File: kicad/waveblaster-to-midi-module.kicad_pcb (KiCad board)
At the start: 2 copper layers, 33 x 101 mm, 14 parts, among them J1 Midi Out, J2 Midi In, J3 Right In, J4 Left In, J5 Right Out, J6 Left Out, J7 Wavetable Input, U1 H11L1

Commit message: final board revision, update readme
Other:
- board text added: "Waveblaster Breakout Card v1.0 by Nikitalita"
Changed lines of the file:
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@@
     (property "Sheetfile" "waveblaster-to-midi-module.kicad_sch")
     (property "Sheetname" "")
-    (attr exclude_from_pos_files)
+    (attr exclude_from_pos_files exclude_from_bom)
     (fp_text reference "H1" (at 0 -4.2) (layer "F.SilkS") hide
       (effects (font (size 1 1) (thickness 0.15)))
@@
     (property "Sheetfile" "waveblaster-to-midi-module.kicad_sch")
     (property "Sheetname" "")
-    (attr through_hole)
+    (attr through_hole exclude_from_pos_files exclude_from_bom)
     (fp_text reference "U1" (at -0.01 -5.6 270) (layer "F.SilkS")
       (effects (font (size 1 1) (thickness 0.15)))
@@
     (property "Sheetfile" "waveblaster-to-midi-module.kicad_sch")
     (property "Sheetname" "")
-    (attr through_hole)
+    (attr through_hole exclude_from_pos_files exclude_from_bom)
     (fp_text reference "D1" (at 7.0893 0.08 270) (layer "F.SilkS")
       (effects (font (size 1 1) (thickness 0.15)))
@@
     (property "Sheetfile" "waveblaster-to-midi-module.kicad_sch")
     (property "Sheetname" "")
-    (attr through_hole)
+    (attr through_hole exclude_from_pos_files exclude_from_bom)
     (fp_text reference "J2" (at 0.1 -6.45 90) (layer "F.SilkS")
       (effects (font (size 1 1) (thickness 0.15)))
@@
     (property "Sheetfile" "waveblaster-to-midi-module.kicad_sch")
     (property "Sheetname" "")
-    (attr through_hole)
+    (attr through_hole exclude_from_pos_files exclude_from_bom)
     (fp_text reference "R2" (at -2.03 -0.01 90) (layer "F.SilkS")
       (effects (font (size 1 1) (thickness 0.15)))
@@
     (property "Sheetfile" "waveblaster-to-midi-module.kicad_sch")
     (property "Sheetname" "")
-    (attr through_hole)
+    (attr through_hole exclude_from_pos_files exclude_from_bom)
     (fp_text reference "J5" (at -5.43 -6.03) (layer "F.SilkS")
       (effects (font (size 1.006465 1.006465) (thickness 0.15)))
@@
     (pad "2" thru_hole oval (at -8.5 0) (size 3.4 1.7) (drill oval 2.3 1) (layers *.Cu *.Mask)
       (net 15 "WT_AUDIO_R_IN") (pintype "passive"))
-    (model "${KIPRJMOD}/Library.3dshapes/CUI_DEVICES_RCJ-042.step"
+    (model "${KIPRJMOD}/Library.3dshapes/CUI_DEVICES_RCJ-042.step" hide
       (offset (xyz -10.1 0 6.5))
       (scale (xyz 1 1 1))
@@
     (property "Sheetfile" "waveblaster-to-midi-module.kicad_sch")
     (property "Sheetname" "")
-    (attr through_hole)
+    (attr through_hole exclude_from_pos_files exclude_from_bom)
     (fp_text reference "R1" (at -1.79 -0.34) (layer "F.SilkS")
       (effects (font (size 1 1) (thickness 0.15)))
@@
     (property "Sheetfile" "waveblaster-to-midi-module.kicad_sch")
     (property "Sheetname" "")
-    (attr through_hole)
+    (attr through_hole exclude_from_pos_files exclude_from_bom)
     (fp_text reference "J6" (at -5.27 -5.93) (layer "F.SilkS")
       (effects (font (size 1.006465 1.006465) (thickness 0.15)))
@@
     (pad "2" thru_hole oval (at -8.5 0) (size 3.4 1.7) (drill oval 2.3 1) (layers *.Cu *.Mask)
       (net 12 "WT_AUDIO_L_IN") (pintype "passive"))
-    (model "${KIPRJMOD}/Library.3dshapes/CUI_DEVICES_RCJ-043.step"
+    (model "${KIPRJMOD}/Library.3dshapes/CUI_DEVICES_RCJ-043.step" hide
       (offset (xyz -10.1 0 6.5))
       (scale (xyz 1 1 1))
@@
       (xy 156.98 153)
     ) (layer "Edge.Cuts") (width 0.1) (fill none))
+  (gr_text "Waveblaster Breakout Card\nv1.0\nby Nikitalita" (at 162.48 135.11 90) (layer "B.SilkS")
+    (effects (font (size 1.5 1.5) (thickness 0.3)) (justify mirror))
+  )
   (gr_text "2" (at 160.29 87.01 90) (layer "B.SilkS")
     (effects (font (size 1 1) (thickness 0.15)) (justify mirror))

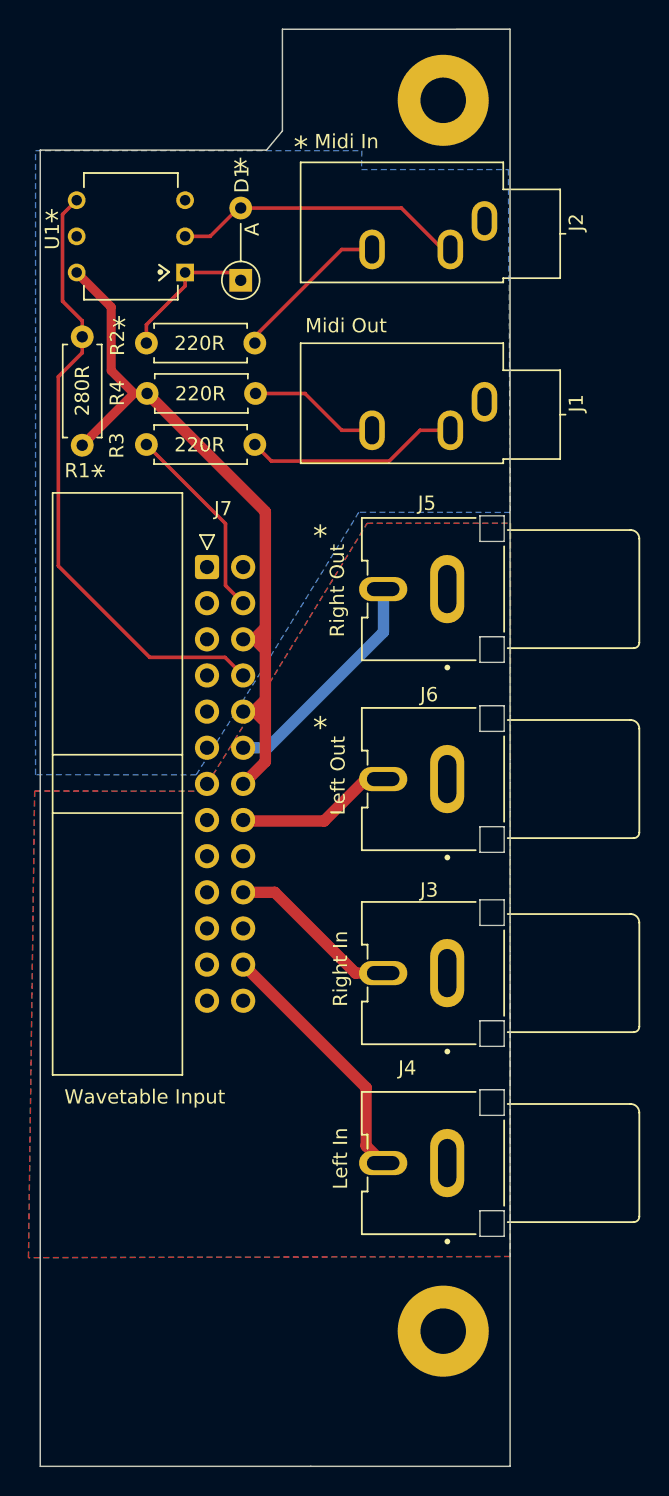
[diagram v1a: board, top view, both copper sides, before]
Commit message: Adjust outline of PCB, finalize bracket
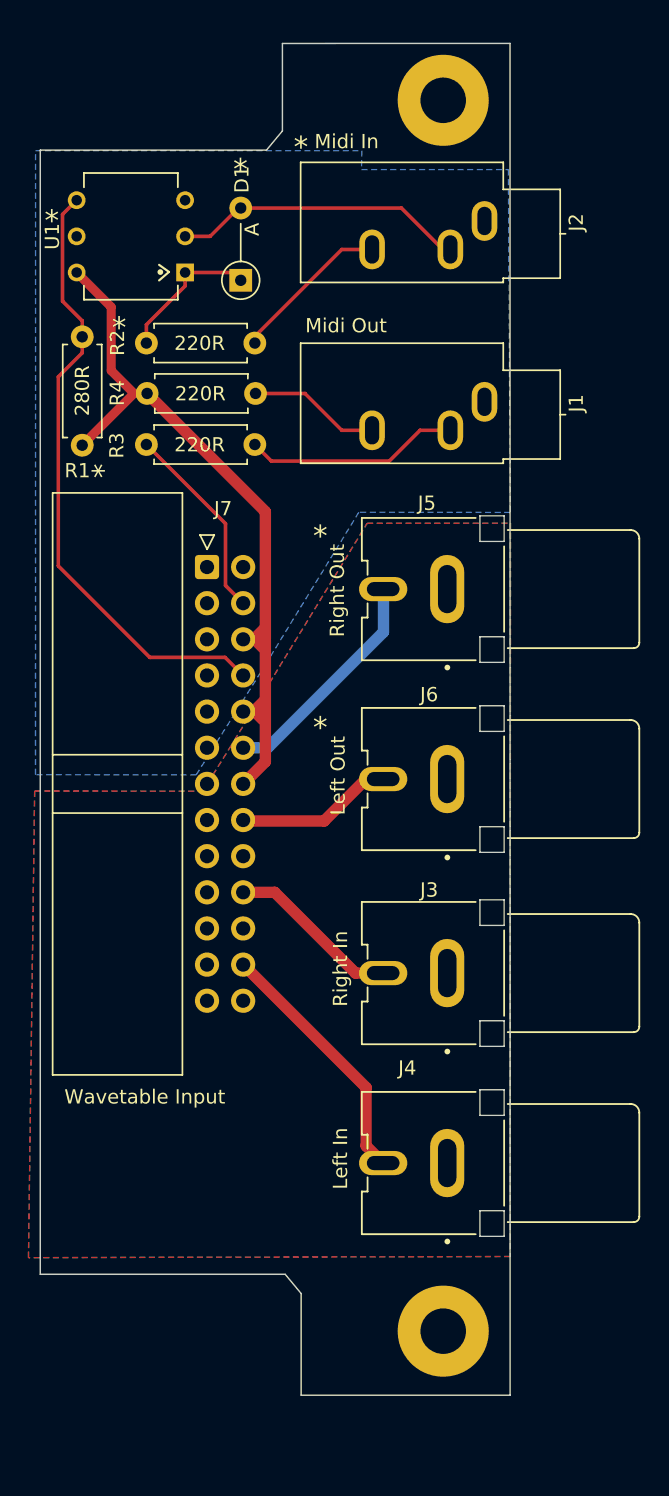
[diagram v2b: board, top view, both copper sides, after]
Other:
- board size 33 x 101 mm -> 33 x 95 mm
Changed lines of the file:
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@@
   (gr_line (start 159.09 95.51) (end 159.09 96.01) (layer "B.SilkS") (width 0.15))
   (gr_line (start 164.2 88) (end 159.1 88) (layer "B.SilkS") (width 0.1))
-  (gr_line (start 218.435 164.47) (end 218.435 168.28) (layer "Cmts.User") (width 0.15))
-  (gr_line (start 200.02 164.47) (end 200.02 168.28) (layer "Cmts.User") (width 0.15))
-  (gr_line (start 211.7675 50.17) (end 211.7675 55.504) (layer "Cmts.User") (width 0.15))
-  (gr_line (start 197.48 59.6315) (end 201.6075 55.504) (layer "Cmts.User") (width 0.15))
-  (gr_line (start 215.895 59.6315) (end 215.895 161.93) (layer "Cmts.User") (width 0.15))
-  (gr_line (start 218.435 168.28) (end 200.02 168.28) (layer "Cmts.User") (width 0.15))
-  (gr_line (start 197.48 161.93) (end 197.48 59.6315) (layer "Cmts.User") (width 0.15))
-  (gr_arc (start 209.8625 48.265) (mid 211.209538 48.822962) (end 211.7675 50.17) (layer "Cmts.User") (width 0.15))
-  (gr_line (start 197.48 161.93) (end 200.02 164.47) (layer "Cmts.User") (width 0.15))
-  (gr_line (start 209.8625 48.265) (end 203.5125 48.265) (layer "Cmts.User") (width 0.15))
-  (gr_circle (center 206.6875 147.325) (end 202.9375 147.325) (layer "Cmts.User") (width 0.15) (fill none))
-  (gr_line (start 215.895 161.93) (end 218.435 164.47) (layer "Cmts.User") (width 0.15))
-  (gr_line (start 211.7675 55.504) (end 215.895 59.6315) (layer "Cmts.User") (width 0.15))
-  (gr_line (start 201.6075 55.504) (end 201.6075 50.17) (layer "Cmts.User") (width 0.15))
-  (gr_arc (start 201.6075 50.17) (mid 202.165462 48.822962) (end 203.5125 48.265) (layer "Cmts.User") (width 0.15))
-  (gr_poly
-    (pts
-      (xy 176 153)
-      (xy 190 153)
-      (xy 189.995606 52)
-      (xy 174 52.004424)
-      (xy 174 59.15)
-      (xy 172.88 60.5)
-      (xy 156.98 60.5)
-      (xy 156.98 153)
-    ) (layer "Edge.Cuts") (width 0.1) (fill none))
-  (gr_text "Waveblaster Breakout Card\nv1.0\nby Nikitalita" (at 162.48 135.11 90) (layer "B.SilkS")
+  (gr_line (start 218.435 149.47) (end 218.435 153.28) (layer "Cmts.User") (width 0.15))
+  (gr_line (start 200.02 149.47) (end 200.02 153.28) (layer "Cmts.User") (width 0.15))
+  (gr_line (start 211.7675 35.17) (end 211.7675 40.504) (layer "Cmts.User") (width 0.15))
+  (gr_line (start 197.48 44.6315) (end 201.6075 40.504) (layer "Cmts.User") (width 0.15))
+  (gr_line (start 215.895 44.6315) (end 215.895 146.93) (layer "Cmts.User") (width 0.15))
+  (gr_line (start 218.435 153.28) (end 200.02 153.28) (layer "Cmts.User") (width 0.15))
+  (gr_line (start 197.48 146.93) (end 197.48 44.6315) (layer "Cmts.User") (width 0.15))
+  (gr_arc (start 209.8625 33.265) (mid 211.209538 33.822962) (end 211.7675 35.17) (layer "Cmts.User") (width 0.15))
+  (gr_line (start 197.48 146.93) (end 200.02 149.47) (layer "Cmts.User") (width 0.15))
+  (gr_line (start 209.8625 33.265) (end 203.5125 33.265) (layer "Cmts.User") (width 0.15))
+  (gr_circle (center 206.6875 132.325) (end 202.9375 132.325) (layer "Cmts.User") (width 0.15) (fill none))
+  (gr_line (start 215.895 146.93) (end 218.435 149.47) (layer "Cmts.User") (width 0.15))
+  (gr_line (start 211.7675 40.504) (end 215.895 44.6315) (layer "Cmts.User") (width 0.15))
+  (gr_line (start 201.6075 40.504) (end 201.6075 35.17) (layer "Cmts.User") (width 0.15))
+  (gr_arc (start 201.6075 35.17) (mid 202.165462 33.822962) (end 203.5125 33.265) (layer "Cmts.User") (width 0.15))
+  (gr_line (start 190 148) (end 189.995606 53) (layer "Edge.Cuts") (width 0.1))
+  (gr_line (start 172.88 60.5) (end 156.98 60.5) (layer "Edge.Cuts") (width 0.1))
+  (gr_line (start 156.98 60.5) (end 156.98 139.504424) (layer "Edge.Cuts") (width 0.1))
+  (gr_line (start 175.315 148) (end 190 148) (layer "Edge.Cuts") (width 0.1))
+  (gr_line (start 175.315 140.854424) (end 175.315 148) (layer "Edge.Cuts") (width 0.1))
+  (gr_line (start 174 53.004424) (end 174 59.15) (layer "Edge.Cuts") (width 0.1))
+  (gr_line (start 189.995606 53) (end 174 53.004424) (layer "Edge.Cuts") (width 0.1))
+  (gr_line (start 174 59.15) (end 172.88 60.5) (layer "Edge.Cuts") (width 0.1))
+  (gr_line (start 174.195 139.504424) (end 175.315 140.854424) (layer "Edge.Cuts") (width 0.1))
+  (gr_line (start 156.98 139.504424) (end 174.195 139.504424) (layer "Edge.Cuts") (width 0.1))
+  (gr_text "Waveblaster Breakout Card\nv1.0\nby Nikitalita" (at 162.4 122 90) (layer "B.SilkS")
     (effects (font (size 1.5 1.5) (thickness 0.3)) (justify mirror))
   )
